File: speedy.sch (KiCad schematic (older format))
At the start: 49 parts, among them Q1 FDN306P, U1 STM32F415RGT6, U2 NUF2042VX6, U3 MAX3051, X1 16Mhz 10ppm

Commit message: Netlist
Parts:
- C1, C10, C11, C13, C14, C2, C3, C4, C5, C6, C7, C8, C9, F1, F3, R1, R10, R11, R12, R13, R14, R2, R3, R36, R4, R5, R6, R7, R8, R9: footprint (none) -> _std:_0402
- C12: footprint (none) -> _std:_0603
- CONN2: footprint MODULE -> Connectors_Molex:Connector_Molex_PicoBlade_53398-0571
- CONN3: footprint MODULE -> _div:_Molex-microSD-WM6701
- CONN4: footprint (none) -> _connectors:_Micro-USB-AB-receptacle-SMT
- CONN5, CONN6: footprint MODULE -> Connectors_Molex:Connector_Molex_PicoBlade_53398-0471
- D1, D2, D3, D4: footprint (none) -> LEDs:LED-0603
- D5, D6: footprint (none) -> _std:_SOD-323
- Q1: footprint (none) -> _std:SSOT-3
- U1: footprint MODULE -> _lqfp:_LQFP64
- U2: footprint (none) -> _std:SOT-563_6-lead
- U3: footprint (none) -> _std:_SOT23-8
- W1, W2: footprint (none) -> Measurement_Points:Measurement_Point_Square-SMD-Pad_Small
- X1: footprint (none) -> _div:_TSX-3225-SMD-XTAL
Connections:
- net labels removed: VL6180X_GPIO0, VL6180X_GPIO1
- wire segments 205 -> 201
- no-connect marks 3 -> 5

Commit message: Remove CAN interface
(not useful enough, takes too much place)
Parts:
- removed C14: 0.1uF, _std:_0402, symbol C_Small
- removed CONN5, CONN6: CAN, Connectors_Molex:Connector_Molex_PicoBlade_53398-0471, symbol CAN-RESCUE-speedy
- removed D6: SBR130S3-7, _std:_SOD-323, symbol D_Schottky_Small-RESCUE-speedy
- removed F3: 500mA, _std:_0402, symbol F_Small
- removed R36: 0R, _std:_0402, symbol R_Small
- removed U3: MAX3051, _std:_SOT23-8, symbol MAX3051
- W1, W2: footprint Measurement_Points:Measurement_Point_Square-SMD-Pad_Small -> _std:Measurement_Point_Round-SMD-Pad_Small
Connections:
- wire segments 201 -> 178
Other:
- note removed: "CAN Transceiver"
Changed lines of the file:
@@
-	1    0    0    -1
-$EndComp
-$Comp
-L MAX3051 U3
-U 1 1 553BA44B
-P 9425 1700
-F 0 "U3" H 9275 1650 60  0000 C CNN
-F 1 "MAX3051" H 9175 2350 60  0000 C CNN
-F 2 "_std:_SOT23-8" H 9425 1700 60  0001 C CNN
-F 3 "" H 9425 1700 60  0000 C CNN
-	1    9425 1700
-	1    0    0    -1
-$EndComp
-$Comp
-L GND #PWR019
-U 1 1 553BA97C
-P 9000 1600
-F 0 "#PWR019" H 9000 1350 50  0001 C CNN
-F 1 "GND" H 9000 1450 50  0000 C CNN
-F 2 "" H 9000 1600 60  0000 C CNN
-F 3 "" H 9000 1600 60  0000 C CNN
-	1    9000 1600
-	1    0    0    -1
-$EndComp
-$Comp
-L GND #PWR020
-U 1 1 553BA9F4
-P 9575 1900
-F 0 "#PWR020" H 9575 1650 50  0001 C CNN
-F 1 "GND" H 9575 1750 50  0000 C CNN
-F 2 "" H 9575 1900 60  0000 C CNN
-F 3 "" H 9575 1900 60  0000 C CNN
-	1    9575 1900
-	1    0    0    -1
-$EndComp
-$Comp
-L GND #PWR021
-U 1 1 553BAE08
-P 9825 850
-F 0 "#PWR021" H 9825 600 50  0001 C CNN
-F 1 "GND" H 9825 700 50  0000 C CNN
-F 2 "" H 9825 850 60  0000 C CNN
-F 3 "" H 9825 850 60  0000 C CNN
-	1    9825 850
-	1    0    0    -1
-$EndComp
-$Comp
-L VCC #PWR022
-U 1 1 553BB120
-P 9475 800
-F 0 "#PWR022" H 9475 650 50  0001 C CNN
-F 1 "VCC" H 9475 950 50  0000 C CNN
-F 2 "" H 9475 800 60  0000 C CNN
-F 3 "" H 9475 800 60  0000 C CNN
-	1    9475 800
 	1    0    0    -1
 $EndComp
@@
 Text Label 3875 4050 0    39   ~ 0
 CAN1_RX
-Text Label 8825 1500 2    39   ~ 0
-CAN1_TX
-Text Label 8825 1400 2    39   ~ 0
-CAN1_RX
 Text Label 3875 3750 0    39   ~ 0
 CAN1_EN
-Text Label 8825 1200 2    39   ~ 0
-CAN1_EN
-$Comp
-L GND #PWR023
-U 1 1 553C0E61
-P 10450 1250
-F 0 "#PWR023" H 10450 1000 50  0001 C CNN
-F 1 "GND" V 10450 1050 50  0000 C CNN
-F 2 "" H 10450 1250 60  0000 C CNN
-F 3 "" H 10450 1250 60  0000 C CNN
-	1    10450 1250
-	0    1    1    0
-$EndComp
-$Comp
-L GND #PWR024
-U 1 1 553BB8D9
-P 10450 2150
-F 0 "#PWR024" H 10450 1900 50  0001 C CNN
-F 1 "GND" V 10450 1950 50  0000 C CNN
-F 2 "" H 10450 2150 60  0000 C CNN
-F 3 "" H 10450 2150 60  0000 C CNN
-	1    10450 2150
-	0    1    1    0
-$EndComp
 Text Label 10600 4175 0    39   ~ 0
 MOTOR_1_EN
@@
 $EndComp
 $Comp
-L C_Small C14
-U 1 1 5541AE7C
-P 9675 850
-F 0 "C14" V 9750 900 50  0000 L CNN
-F 1 "0.1uF" V 9750 600 50  0000 L CNN
-F 2 "_std:_0402" H 9675 850 60  0001 C CNN
-F 3 "" H 9675 850 60  0000 C CNN
-	1    9675 850
-	0    -1   -1   0
-$EndComp
-$Comp
 L C_Small C10
 U 1 1 5541CCC0
@@
 	1    0    0    -1
 $EndComp
-Text Label 10350 600  2    39   ~ 0
-V_USB
-$Comp
-L D_Schottky_Small-RESCUE-speedy D6
-U 1 1 55457747
-P 10525 725
-F 0 "D6" V 10575 850 50  0000 L CNN
-F 1 "SBR130S3-7" V 10475 775 39  0000 L CNN
-F 2 "_std:_SOD-323" V 10525 725 60  0001 C CNN
-F 3 "" V 10525 725 60  0000 C CNN
-	1    10525 725
-	0    1    -1   0
-$EndComp
-$Comp
-L CAN-RESCUE-speedy CONN5
-U 1 1 553C0701
-P 10925 1300
-F 0 "CONN5" H 10925 1650 50  0000 C CNN
-F 1 "CAN" H 10925 950 50  0000 C CNN
-F 2 "Connectors_Molex:Connector_Molex_PicoBlade_53398-0471" H 11175 1300 50  0001 C CNN
-F 3 "DOCUMENTATION" H 11175 1300 50  0001 C CNN
-	1    10925 1300
-	1    0    0    -1
-$EndComp
 $Comp
 L D_Schottky_Small-RESCUE-speedy D5
@@
 Text Notes 6125 2575 0    60   ~ 0
 SWD interface
-Text Notes 8800 2425 0    60   ~ 0
-CAN Transceiver
 Text Notes 8075 2850 0    60   ~ 0
 USB Termination
@@
 F 0 "W1" H 4275 3875 28  0000 C CNN
 F 1 "TEST" H 4125 3850 20  0000 C CNN
-F 2 "Measurement_Points:Measurement_Point_Square-SMD-Pad_Small" H 4125 3850 60  0001 C CNN
+F 2 "_std:Measurement_Point_Round-SMD-Pad_Small" H 4125 3850 60  0001 C CNN
 F 3 "" H 4125 3850 60  0000 C CNN
 	1    4125 3850
@@
 F 0 "W2" H 4350 3975 28  0000 C CNN
 F 1 "TEST" H 4200 3950 20  0000 C CNN
-F 2 "Measurement_Points:Measurement_Point_Square-SMD-Pad_Small" H 4200 3950 60  0001 C CNN
+F 2 "_std:Measurement_Point_Round-SMD-Pad_Small" H 4200 3950 60  0001 C CNN
 F 3 "" H 4200 3950 60  0000 C CNN
 	1    4200 3950
@@
 Wire Wire Line
 	10600 4175 10550 4175
-Connection ~ 9975 1450
-Wire Wire Line
-	9975 2350 10575 2350
-Wire Wire Line
-	9975 1450 9975 2350
-Connection ~ 10075 1350
-Wire Wire Line
-	10075 1150 10075 2250
-Wire Wire Line
-	10075 2250 10575 2250
-Wire Wire Line
-	10075 1350 10575 1350
-Wire Wire Line
-	9925 1450 10575 1450
-Wire Wire Line
-	9925 1150 10075 1150
 Wire Wire Line
 	3875 3750 3825 3750
 Wire Wire Line
-	9075 1500 8825 1500
-Wire Wire Line
-	8825 1400 9075 1400
-Wire Wire Line
 	4450 7100 4450 7200
-Connection ~ 9475 850
-Wire Wire Line
-	9775 850  9825 850
-Wire Wire Line
-	9475 800  9475 950
-Wire Wire Line
-	9575 850  9475 850
-Wire Wire Line
-	9000 1600 9075 1600
-Wire Wire Line
-	9575 1900 9575 1850
 Connection ~ 5175 6150
 Wire Wire Line
@@
 Wire Wire Line
 	10025 3125 10075 3125
-Wire Wire Line
-	10525 1075 10525 2050
-Wire Wire Line
-	10525 1150 10575 1150
-Wire Wire Line
-	10525 2050 10575 2050
 Wire Wire Line
 	9975 2850 10025 2850
@@
 Wire Wire Line
 	6850 3225 7100 3225
-$Comp
-L R_Small R36
-U 1 1 5591D621
-P 8975 1200
-F 0 "R36" V 9050 1125 50  0000 L CNN
-F 1 "0R" V 8975 1150 50  0000 L CNN
-F 2 "_std:_0402" H 8975 1200 60  0001 C CNN
-F 3 "" H 8975 1200 60  0000 C CNN
-	1    8975 1200
-	0    1    1    0
-$EndComp
-Wire Wire Line
-	8825 1200 8875 1200
-$Comp
-L CAN-RESCUE-speedy CONN6
-U 1 1 553BB83D
-P 10925 2200
-F 0 "CONN6" H 10925 2550 50  0000 C CNN
-F 1 "CAN" H 10925 1850 50  0000 C CNN
-F 2 "Connectors_Molex:Connector_Molex_PicoBlade_53398-0471" H 11175 2200 50  0001 C CNN
-F 3 "DOCUMENTATION" H 11175 2200 50  0001 C CNN
-	1    10925 2200
-	1    0    0    -1
-$EndComp
-Wire Wire Line
-	10450 1250 10575 1250
-Wire Wire Line
-	10450 2150 10575 2150
-Connection ~ 10525 1150
-$Comp
-L F_Small F3
-U 1 1 55921BF2
-P 10525 975
-F 0 "F3" H 10485 1035 50  0000 L CNN
-F 1 "500mA" H 10405 915 50  0000 L CNN
-F 2 "_std:_0402" H 10525 975 60  0001 C CNN
-F 3 "" H 10525 975 60  0000 C CNN
-	1    10525 975
-	0    1    1    0
-$EndComp
-Wire Wire Line
-	10350 600  10525 600
-Wire Wire Line
-	10525 600  10525 625
-Wire Wire Line
-	10525 825  10525 875
 NoConn ~ 3825 1650
 NoConn ~ 3825 1550

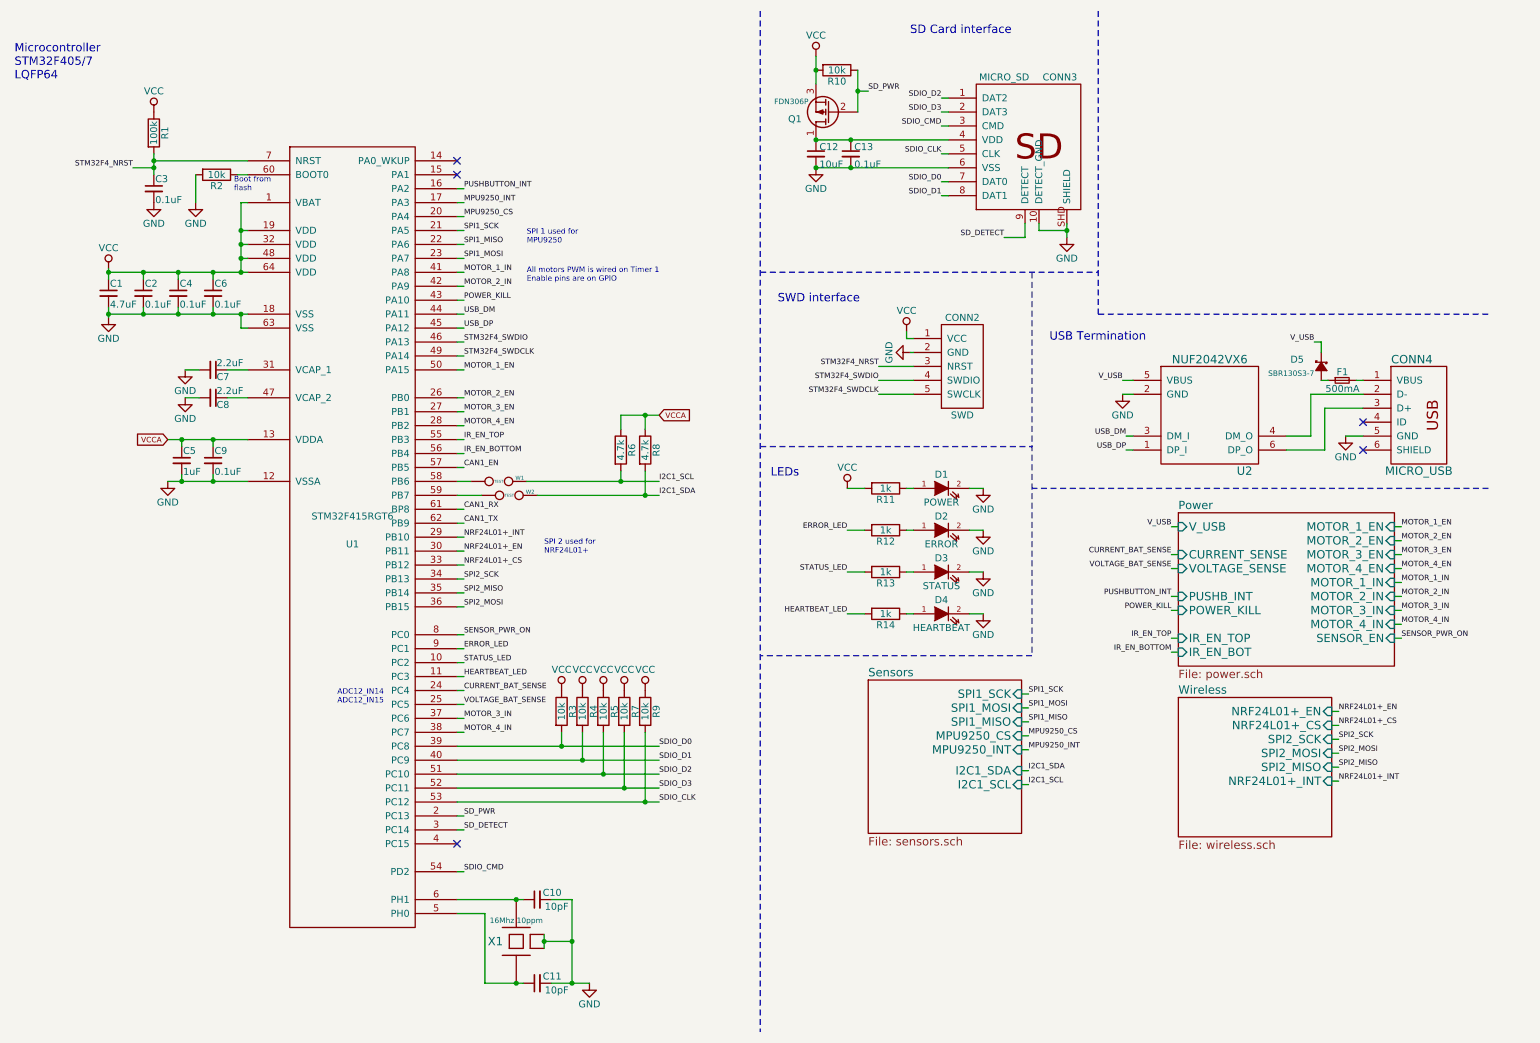
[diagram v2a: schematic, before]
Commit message: Use JTAG instead of SWD
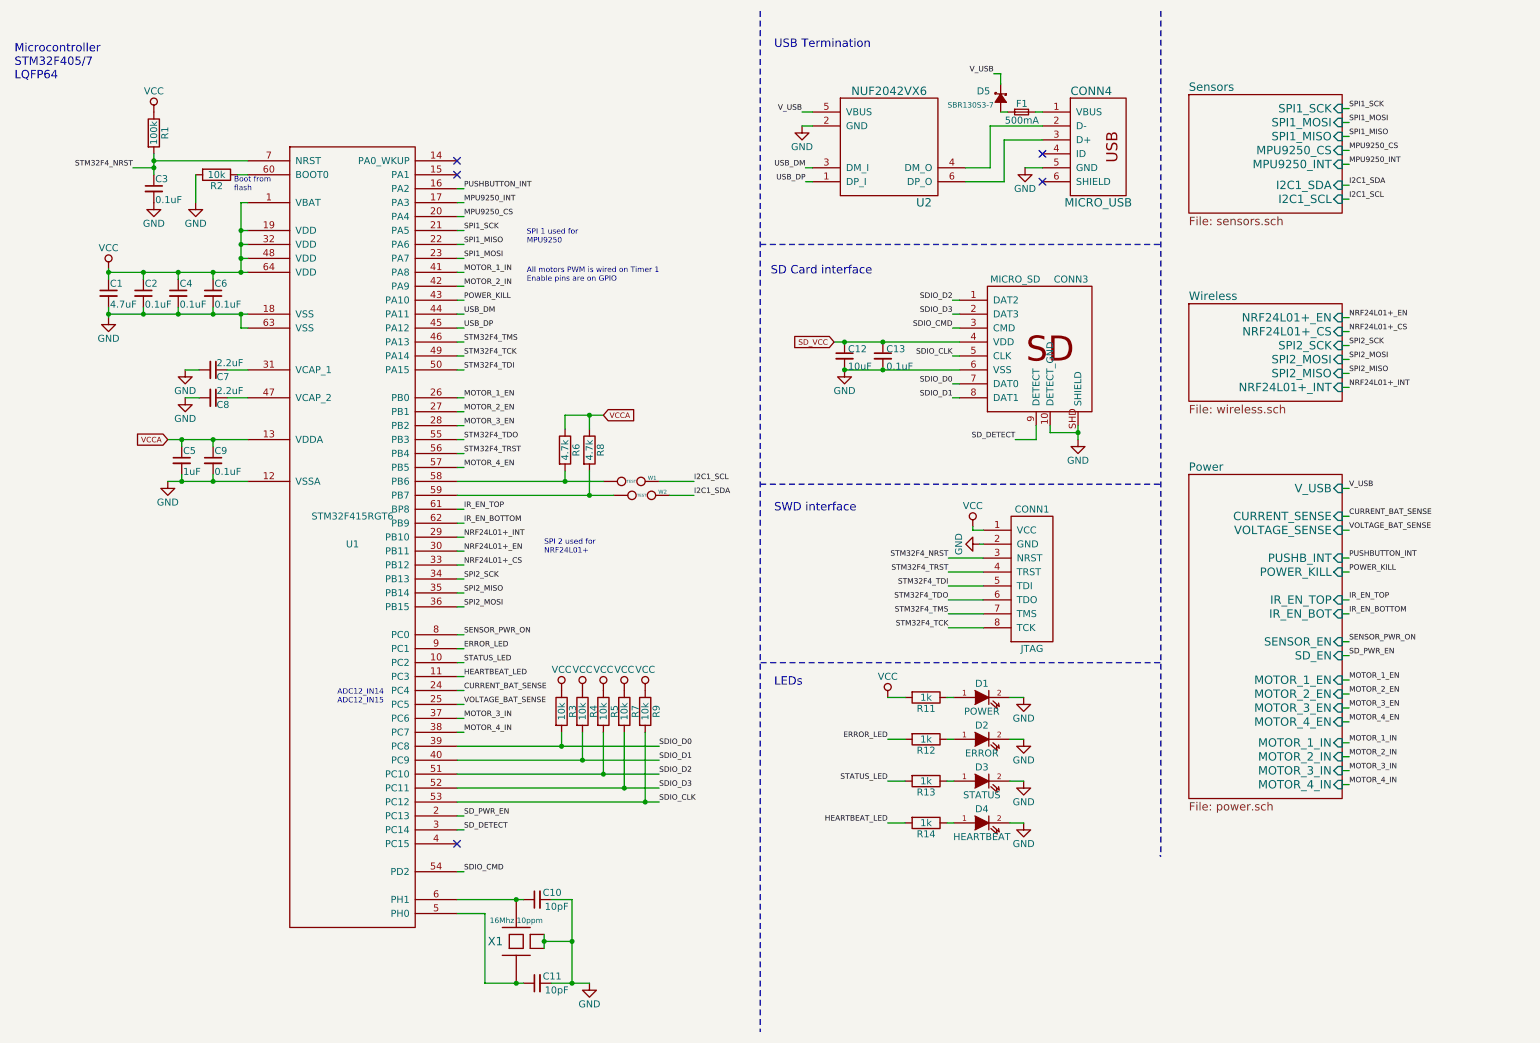
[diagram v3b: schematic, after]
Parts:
- removed CONN2: SWD, Connectors_Molex:Connector_Molex_PicoBlade_53398-0571, symbol SWD
- removed Q1: FDN306P, _std:SSOT-3, symbol Q_PMOS_DGS-RESCUE-speedy
- removed R10: 10k, _std:_0402, symbol R
- added CONN1: JTAG, MODULE, symbol JTAG
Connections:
- net CAN1_EN is gone; now on net MOTOR_4_EN: U1.57 (PB5)
- net CAN1_RX is gone; now on net IR_EN_TOP: U1.61 (BP8)
- net CAN1_TX is gone; now on net IR_EN_BOTTOM: U1.62 (PB9)
- net GND: now also CONN1.2 (GND), CONN1.MECH (GND)
- net I2C1_SCL: no longer R6.2
- net I2C1_SDA: no longer R8.2
- net IR_EN_BOTTOM: no longer U1.56 (PB4)
- net IR_EN_TOP: no longer U1.55 (PB3)
- net MOTOR_1_EN: now also U1.26 (PB0); no longer U1.50 (PA15)
- net MOTOR_2_EN: now also U1.27 (PB1); no longer U1.26 (PB0)
- net MOTOR_3_EN: now also U1.28 (PB2); no longer U1.27 (PB1)
- net MOTOR_4_EN: no longer U1.28 (PB2)
- net STM32F4_NRST: now also CONN1.3 (NRST)
- net VCC: now also CONN1.1 (VCC)
- net SD_VCC: now reaches C12.1, C13.1, CONN3.4 (VDD)
- net at U1.58 (PB6), W1.1: now also R6.2
- net at U1.59 (PB7), W2.1: now also R8.2
- net SD_PWR renamed SD_PWR_EN
- net STM32F4_SWDCLK renamed STM32F4_TCK
- net STM32F4_TCK: now also CONN1.8 (TCK)
- net STM32F4_SWDIO renamed STM32F4_TMS
- net STM32F4_TMS: now also CONN1.7 (TMS)
- new net STM32F4_TDI: CONN1.5 (TDI), U1.50 (PA15)
- new net STM32F4_TDO: CONN1.6 (TDO), U1.55 (PB3)
- new net STM32F4_TRST: CONN1.4 (TRST), U1.56 (PB4)
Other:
- moved on the sheet: C12, C13, CONN3, CONN4, D1, D2, D3, D4, D5, F1, R11, R12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

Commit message: Remove SD card
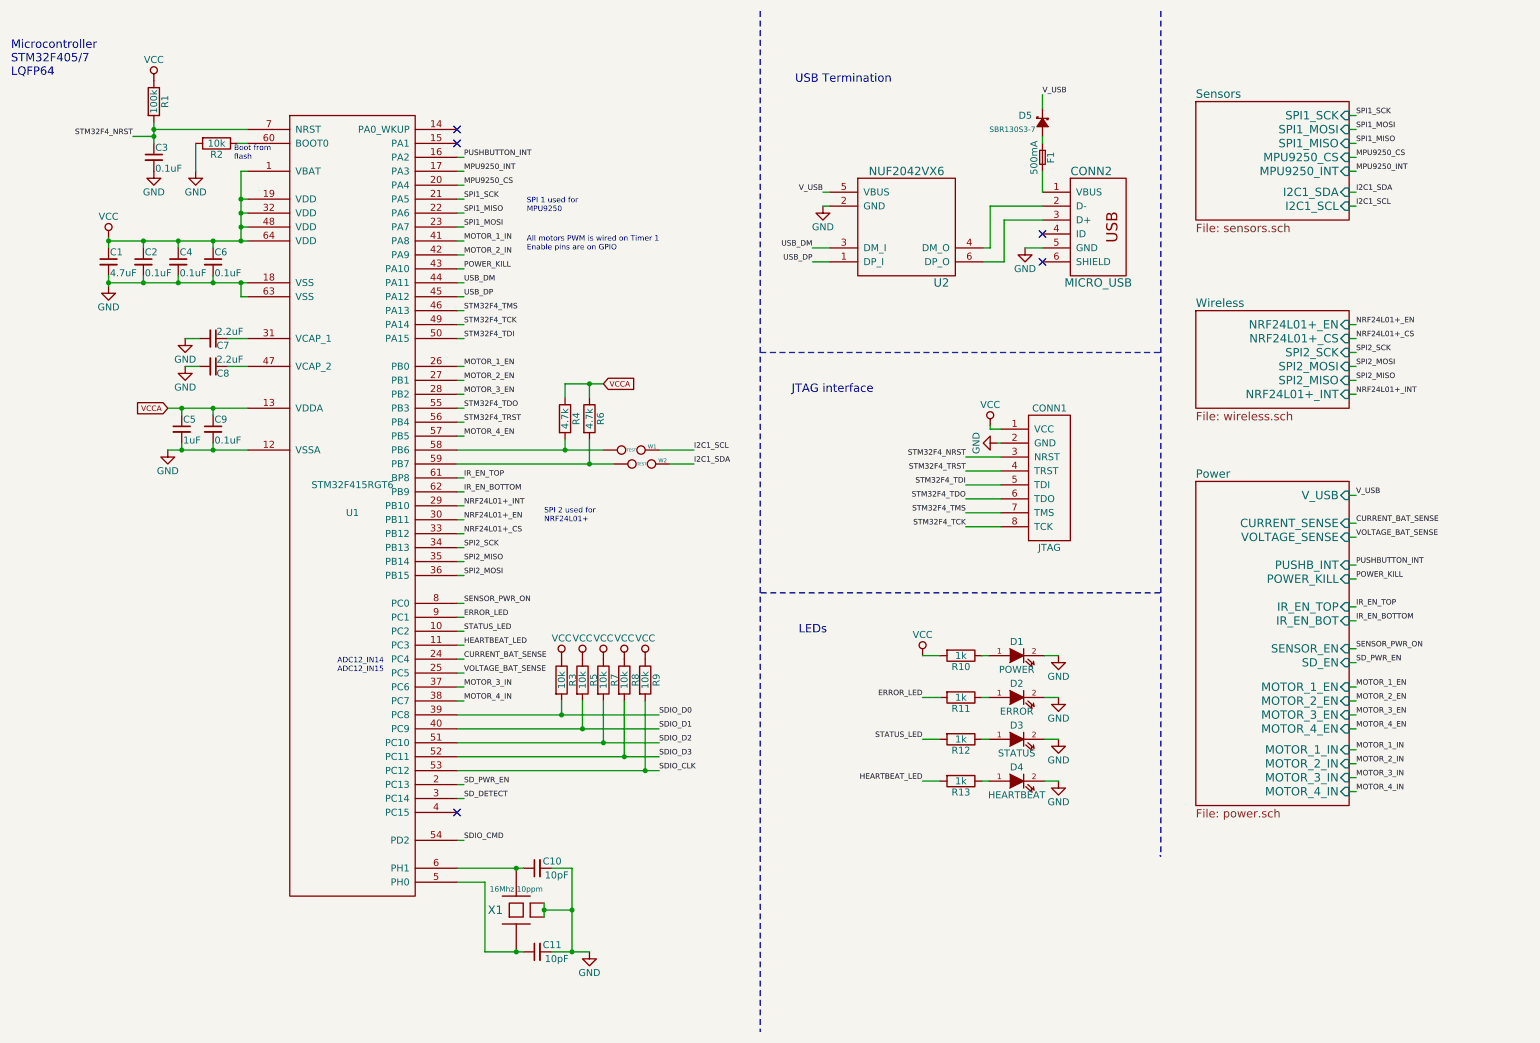
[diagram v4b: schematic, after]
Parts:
- removed C12: 10uF, _std:_0603, symbol C_Small
- removed C13: 0.1uF, _std:_0402, symbol C_Small
- removed CONN3: MICRO_SD, _div:_Molex-microSD-WM6701, symbol MICRO_SD
- CONN1: footprint MODULE -> _connectors:_Molex-PicoBlade-SMD-8
- renumbered CONN4 to CONN2, R11 to R10, R12 to R11, R13 to R12, R14 to R13, R6 to R4, R4 to R5, R8 to R6, R5 to R7, R7 to R8
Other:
- note added: "JTAG interface"
- note removed: "SD Card interface"
- note removed: "SWD interface"
- moved on the sheet: C1, C10, C11, C2, C3, C4, C5, C6, C7, C8, C9, CONN1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

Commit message: Revert "Remove SD card"
This reverts commit 4a1918bee256f93cb8d66746410e6c192988175c.
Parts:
- added C12: 10uF, _std:_0603, symbol C_Small
- added C13: 0.1uF, _std:_0402, symbol C_Small
- added CONN3: MICRO_SD, _div:_Molex-microSD-WM6701, symbol MICRO_SD
- CONN1: footprint _connectors:_Molex-PicoBlade-SMD-8 -> MODULE
- renumbered CONN2 to CONN4, R10 to R11, R11 to R12, R12 to R13, R13 to R14, R5 to R4, R7 to R5, R4 to R6, R8 to R7, R6 to R8
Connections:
- net GND: now also C12.2, C13.2, CONN3.10 (DETECT_GND), CONN3.6 (VSS), CONN3.SHD (SHIELD)
- net SDIO_CLK: now also CONN3.5 (CLK)
- net SDIO_CMD: now also CONN3.3 (CMD)
- net SDIO_D0: now also CONN3.7 (DAT0)
- net SDIO_D1: now also CONN3.8 (DAT1)
- net SDIO_D2: now also CONN3.1 (DAT2)
- net SDIO_D3: now also CONN3.2 (DAT3)
- net SD_DETECT: now also CONN3.9 (DETECT)
- new net SD_VCC: C12.1, C13.1, CONN3.4 (VDD)
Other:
- note added: "SD Card interface"
- note added: "SWD interface"
- note removed: "JTAG interface"
- moved on the sheet: C1, C10, C11, C2, C3, C4, C5, C6, C7, C8, C9, CONN1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
